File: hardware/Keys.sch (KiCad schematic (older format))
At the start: 1 part, among them U2 MCP23018_SSOP

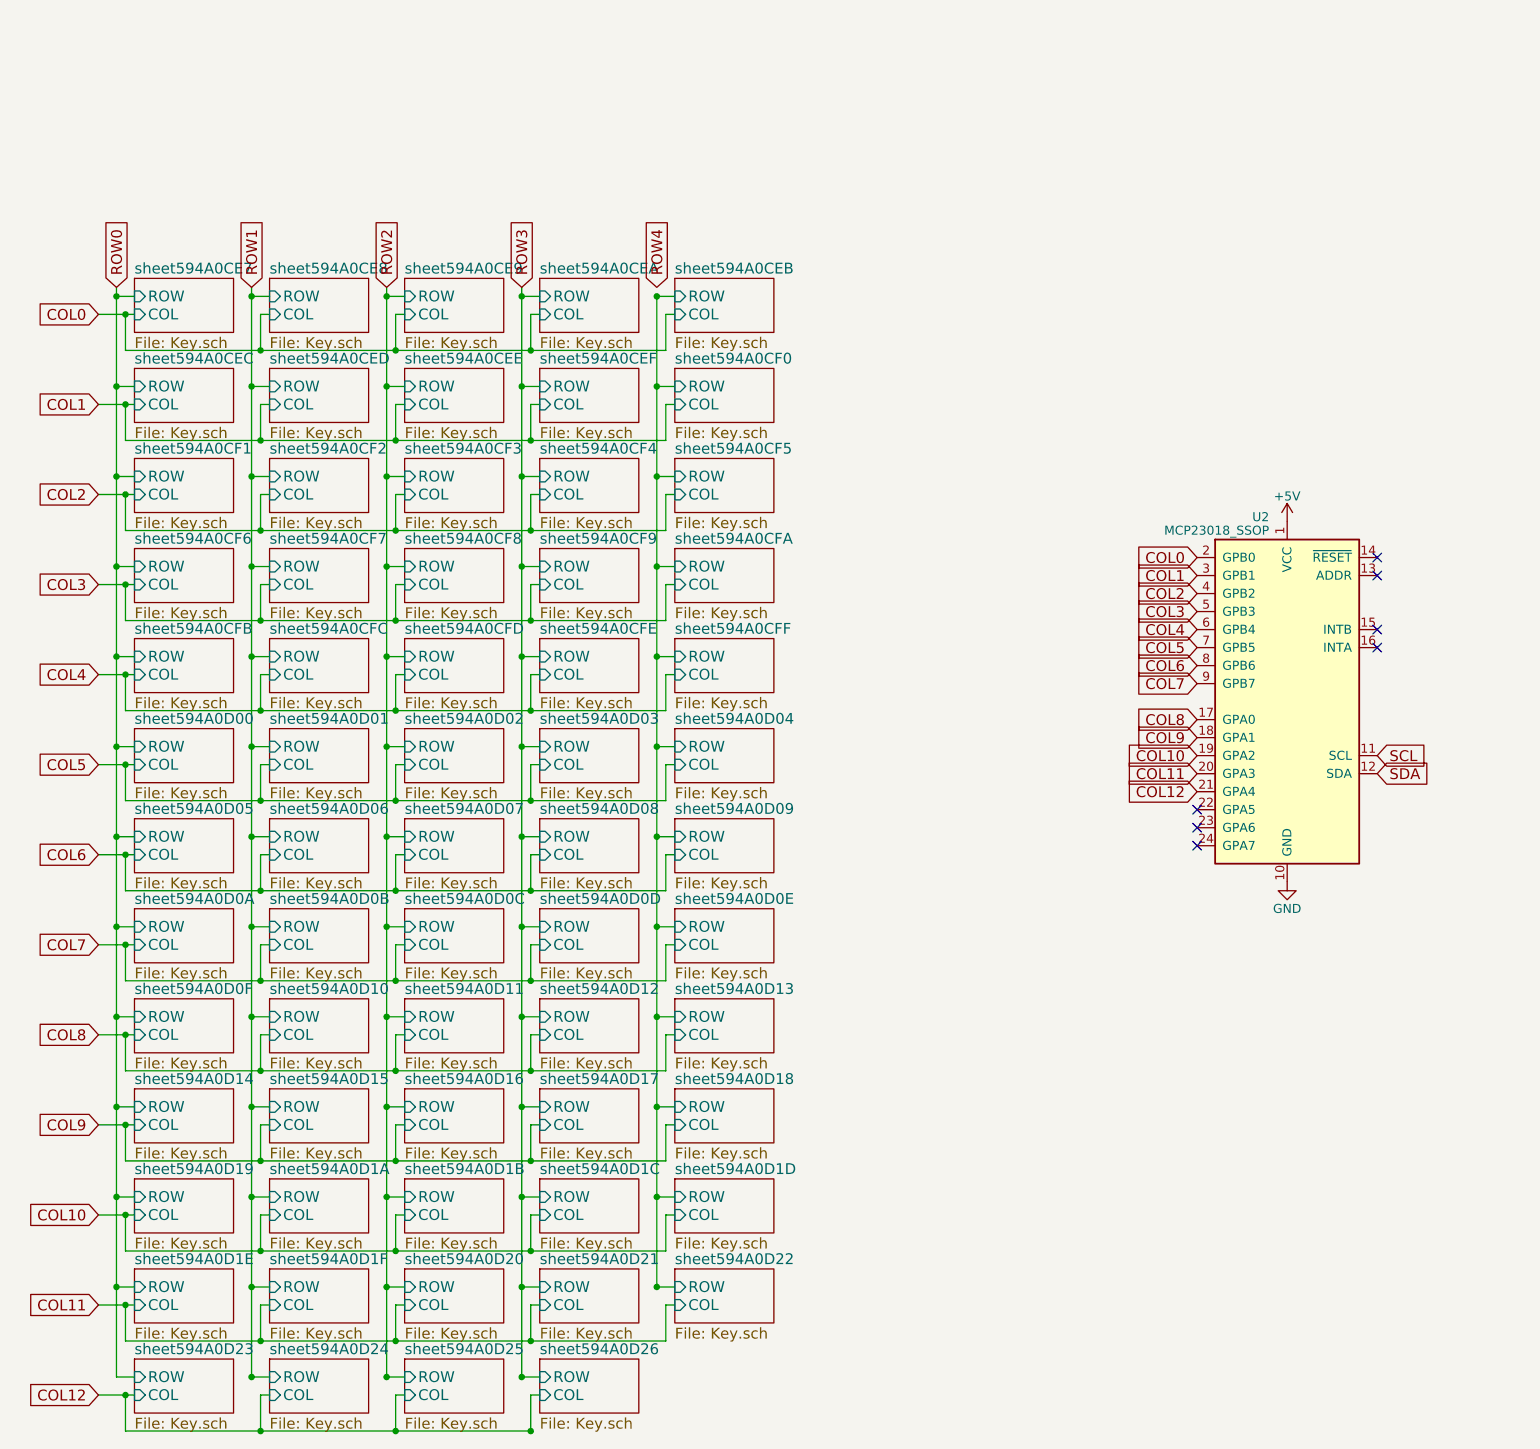
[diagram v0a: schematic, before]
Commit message: Add HWB, breakouts, LED to sch
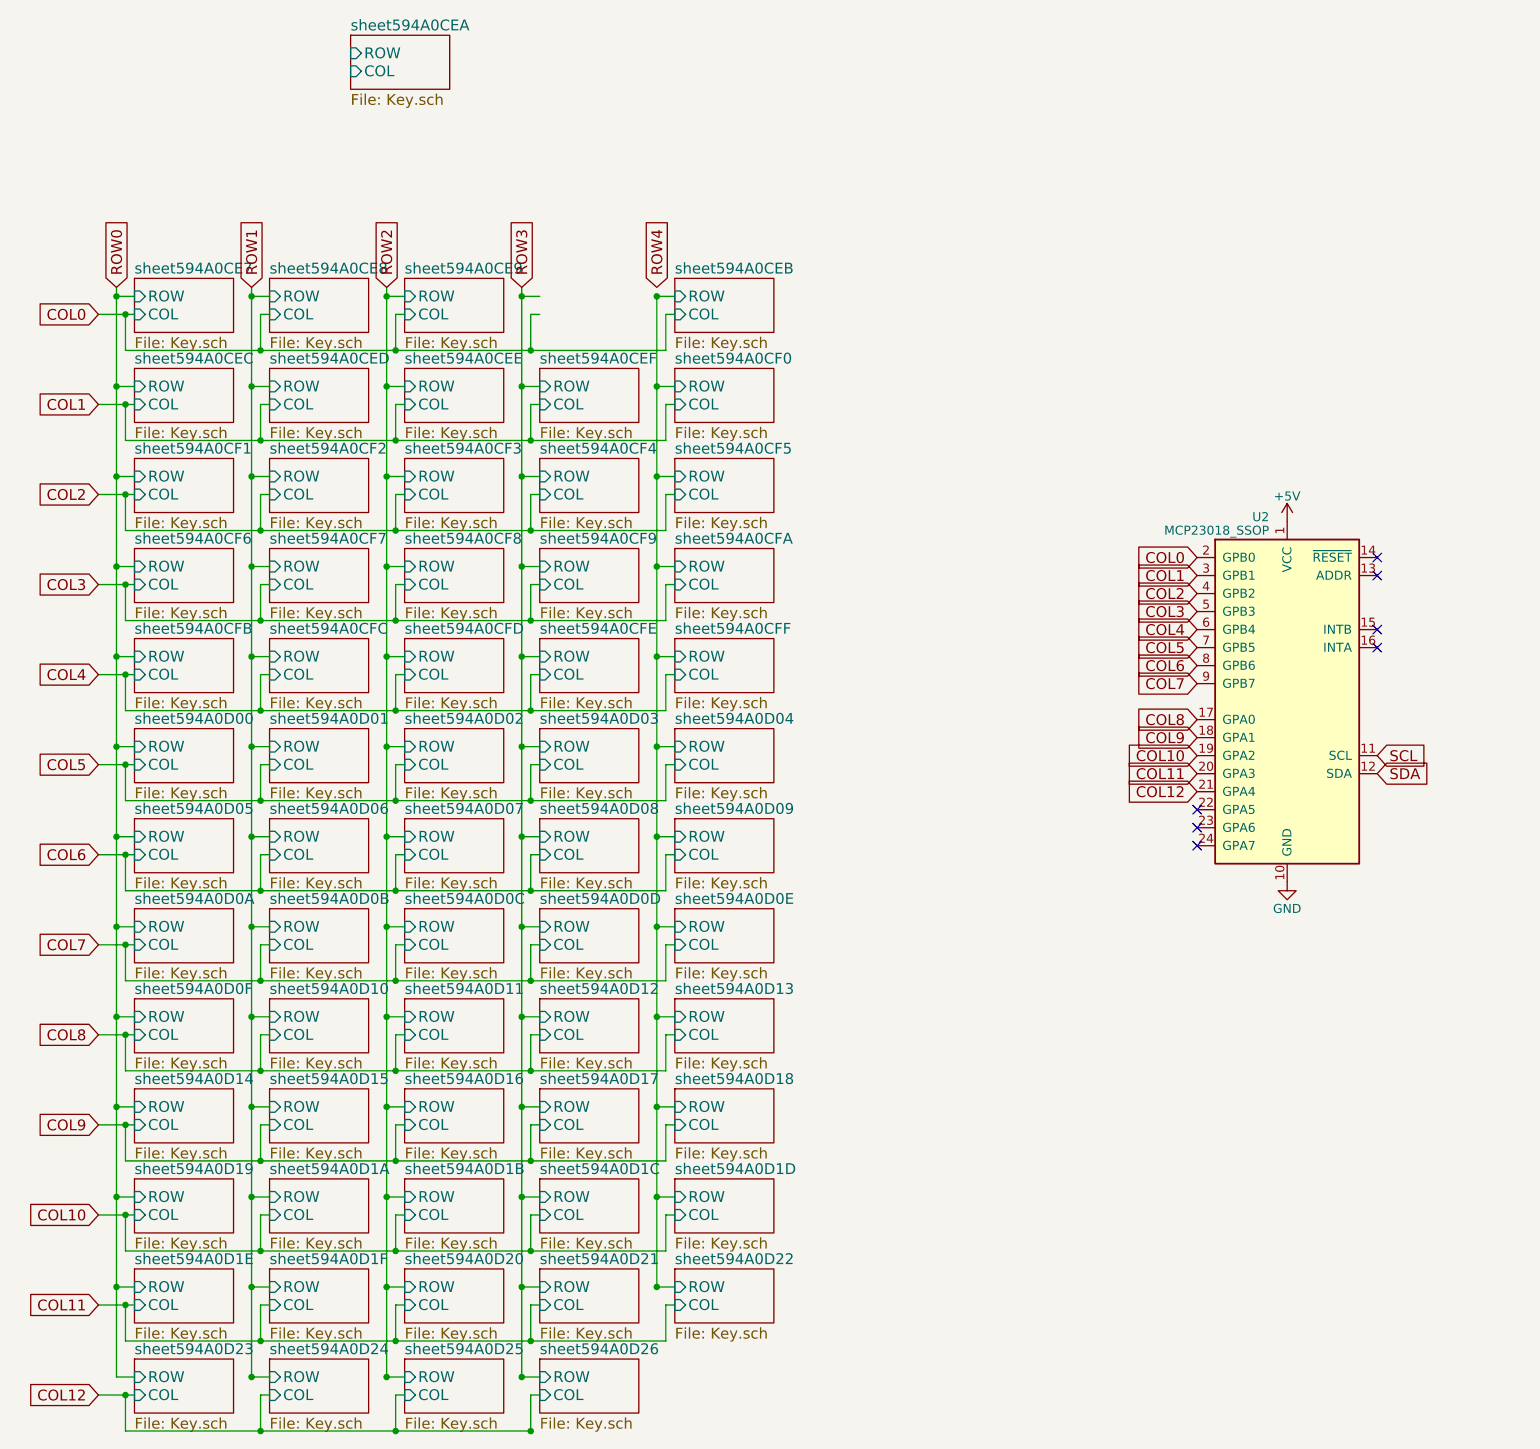
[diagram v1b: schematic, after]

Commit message: Move diodes in script, add big thumb buttons
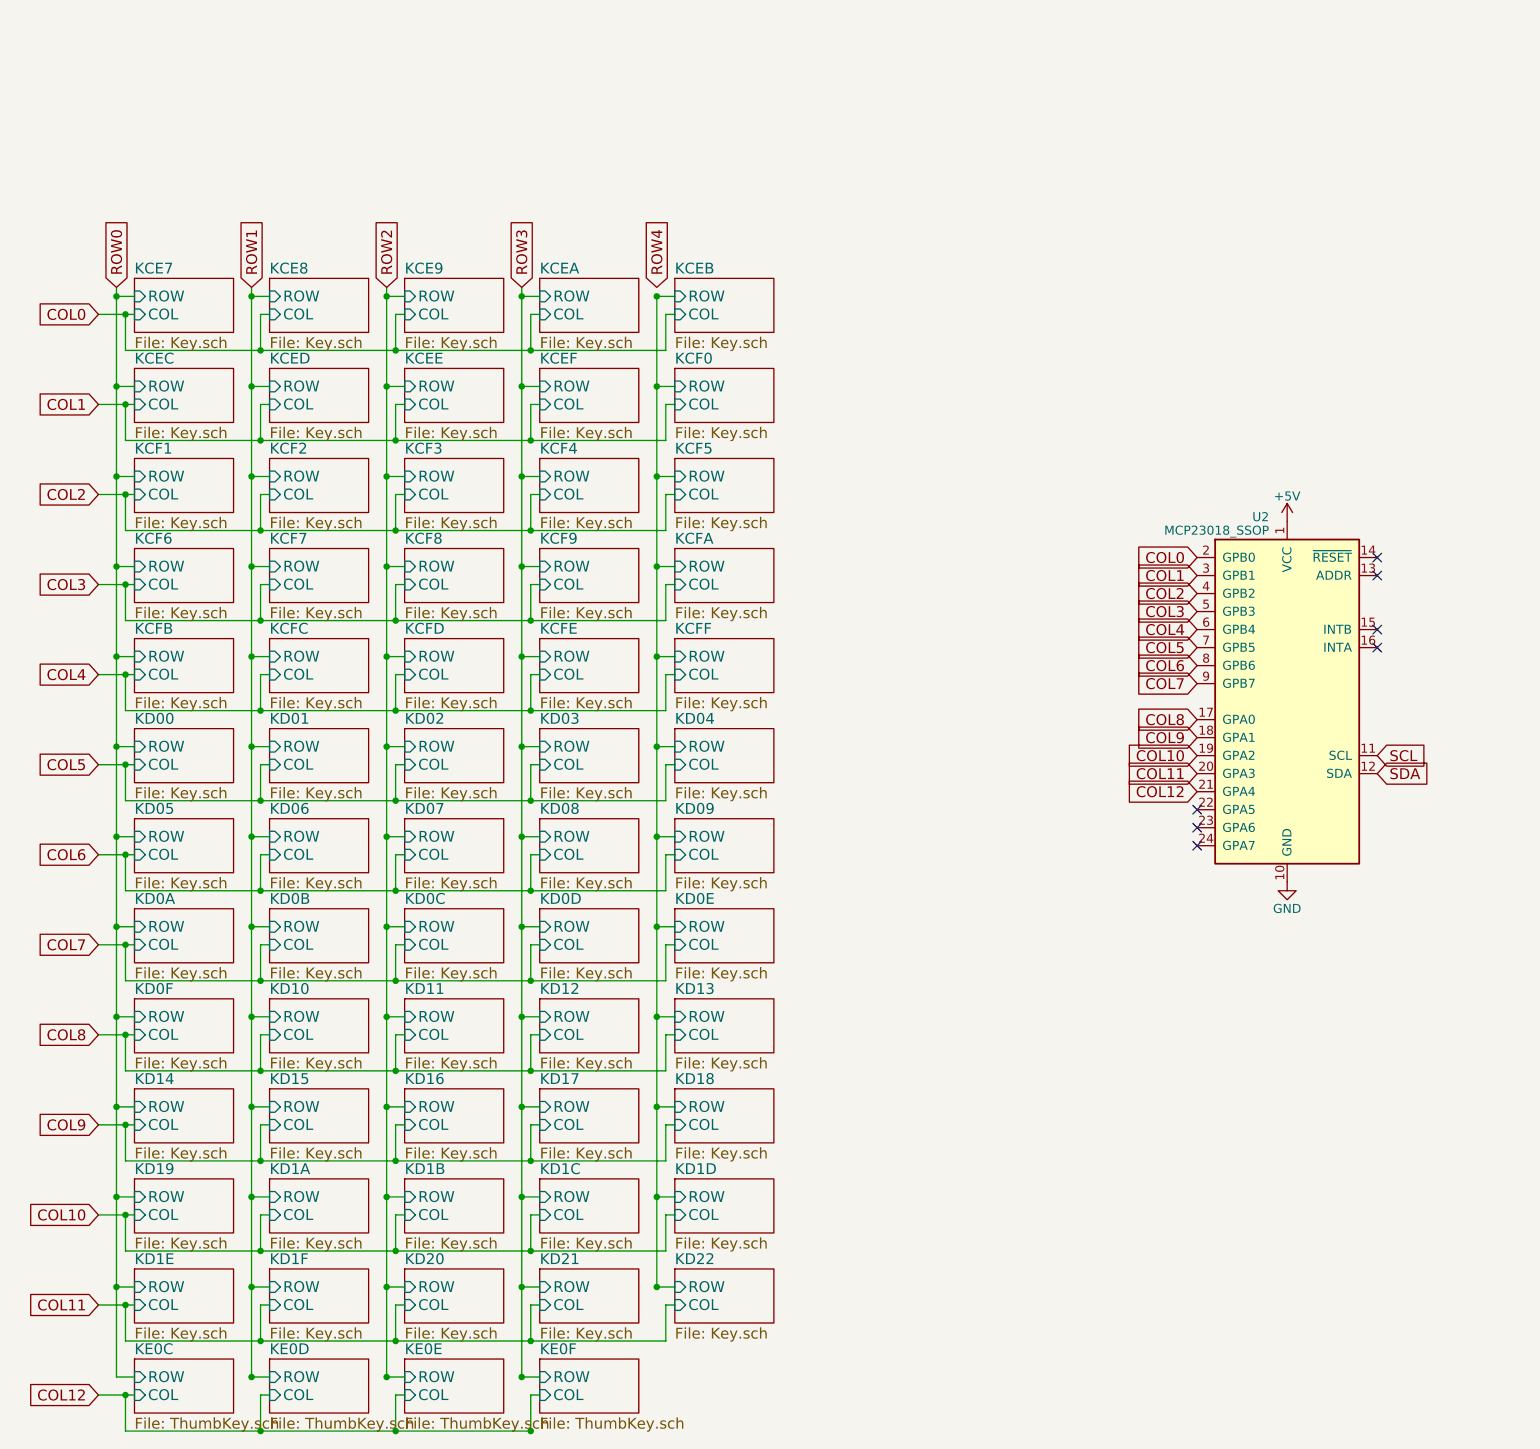
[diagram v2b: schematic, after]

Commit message: Fix diodes, Add board edge
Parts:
- added C5: 100nF, Capacitors_SMD:C_1206_HandSoldering, symbol C_Small
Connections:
- net +5V: now also C5.1
- net GND: now also C5.2
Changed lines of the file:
@@
 NoConn ~ 7300 4100
 $Comp
-L +5V #PWR016
+L +5V #PWR19
 U 1 1 594A3201
 P 7800 2300
-F 0 "#PWR016" H 7800 2150 50  0001 C CNN
+F 0 "#PWR19" H 7800 2150 50  0001 C CNN
 F 1 "+5V" H 7800 2440 50  0000 C CNN
 F 2 "" H 7800 2300 50  0001 C CNN
@@
 $EndComp
 $Comp
-L GND #PWR017
+L GND #PWR21
 U 1 1 594A3207
 P 7800 4300
-F 0 "#PWR017" H 7800 4050 50  0001 C CNN
+F 0 "#PWR21" H 7800 4050 50  0001 C CNN
 F 1 "GND" H 7800 4150 50  0000 C CNN
 F 2 "" H 7800 4300 50  0001 C CNN
@@
 F3 "COL" I L 3650 7150 60
 $EndSheet
+$Comp
+L C_Small C5
+U 1 1 5955CA14
+P 8850 2300
+F 0 "C5" H 8860 2370 50  0000 L CNN
+F 1 "100nF" H 8860 2220 50  0000 L CNN
+F 2 "Capacitors_SMD:C_1206_HandSoldering" H 8850 2300 50  0001 C CNN
+F 3 "" H 8850 2300 50  0001 C CNN
+	1    8850 2300
+	1    0    0    -1
+$EndComp
+$Comp
+L +5V #PWR18
+U 1 1 5955CD8D
+P 8850 2200
+F 0 "#PWR18" H 8850 2050 50  0001 C CNN
+F 1 "+5V" H 8850 2340 50  0000 C CNN
+F 2 "" H 8850 2200 50  0001 C CNN
+F 3 "" H 8850 2200 50  0001 C CNN
+	1    8850 2200
+	1    0    0    -1
+$EndComp
+$Comp
+L GND #PWR20
+U 1 1 5955D0A5
+P 8850 2400
+F 0 "#PWR20" H 8850 2150 50  0001 C CNN
+F 1 "GND" H 8850 2250 50  0000 C CNN
+F 2 "" H 8850 2400 50  0001 C CNN
+F 3 "" H 8850 2400 50  0001 C CNN
+	1    8850 2400
+	1    0    0    -1
+$EndComp
 $EndSCHEMATC

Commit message: Start routing
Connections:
- net COL10: now also U2.21 (GPA4); no longer U2.19 (GPA2)
- net COL11: now also U2.22 (GPA5); no longer U2.20 (GPA3)
- net COL12: now also U2.23 (GPA6); no longer U2.21 (GPA4)
- net COL6: now also U2.17 (GPA0); no longer U2.8 (GPB6)
- net COL7: now also U2.18 (GPA1); no longer U2.9 (GPB7)
- net COL8: now also U2.19 (GPA2); no longer U2.17 (GPA0)
- net COL9: now also U2.20 (GPA3); no longer U2.18 (GPA1)
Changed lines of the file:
@@
 Text GLabel 7300 3000 0    60   Input ~ 0
 COL5
-Text GLabel 7300 3100 0    60   Input ~ 0
+Text GLabel 7300 3400 0    60   Input ~ 0
 COL6
-Text GLabel 7300 3200 0    60   Input ~ 0
+Text GLabel 7300 3500 0    60   Input ~ 0
 COL7
-Text GLabel 7300 3400 0    60   Input ~ 0
+Text GLabel 7300 3600 0    60   Input ~ 0
 COL8
-Text GLabel 7300 3500 0    60   Input ~ 0
+Text GLabel 7300 3700 0    60   Input ~ 0
 COL9
-Text GLabel 7300 3600 0    60   Input ~ 0
+Text GLabel 7300 3800 0    60   Input ~ 0
 COL10
-Text GLabel 7300 3700 0    60   Input ~ 0
+Text GLabel 7300 3900 0    60   Input ~ 0
 COL11
-Text GLabel 7300 3800 0    60   Input ~ 0
+Text GLabel 7300 4000 0    60   Input ~ 0
 COL12
-NoConn ~ 7300 3900
-NoConn ~ 7300 4000
 NoConn ~ 7300 4100
 $Comp
@@
 	1    0    0    -1
 $EndComp
+NoConn ~ 7300 3100
+NoConn ~ 7300 3200
 $EndSCHEMATC

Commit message: WIP for V2 fixes
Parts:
- U2: footprint Housings_SSOP:SSOP-28_5.3x10.2mm_Pitch0.65mm -> Housings_SSOP:SSOP-24_5.3x8.2mm_Pitch0.65mm
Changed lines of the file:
@@
 LIBS:valves
 LIBS:keyboard-cache
-EELAYER 26 0
+EELAYER 25 0
 EELAYER END
 $Descr A4 11693 8268
@@
 NoConn ~ 7300 4100
 $Comp
-L +5V #PWR018
+L +5V #PWR015
 U 1 1 594A3201
 P 7800 2300
-F 0 "#PWR018" H 7800 2150 50  0001 C CNN
+F 0 "#PWR015" H 7800 2150 50  0001 C CNN
 F 1 "+5V" H 7800 2440 50  0000 C CNN
 F 2 "" H 7800 2300 50  0001 C CNN
@@
 $EndComp
 $Comp
-L GND #PWR019
+L GND #PWR016
 U 1 1 594A3207
 P 7800 4300
-F 0 "#PWR019" H 7800 4050 50  0001 C CNN
+F 0 "#PWR016" H 7800 4050 50  0001 C CNN
 F 1 "GND" H 7800 4150 50  0000 C CNN
 F 2 "" H 7800 4300 50  0001 C CNN
@@
 F 0 "U2" H 7700 4325 50  0000 R CNN
 F 1 "MCP23018_SSOP" H 7700 4250 50  0000 R CNN
-F 2 "Housings_SSOP:SSOP-28_5.3x10.2mm_Pitch0.65mm" H 7850 2350 50  0001 L CNN
+F 2 "Housings_SSOP:SSOP-24_5.3x8.2mm_Pitch0.65mm" H 7850 2350 50  0001 L CNN
 F 3 "" H 8050 4300 50  0001 C CNN
 	1    7800 3300
@@
 $EndComp
 $Comp
-L +5V #PWR020
+L +5V #PWR017
 U 1 1 5955CD8D
 P 8850 2200
-F 0 "#PWR020" H 8850 2050 50  0001 C CNN
+F 0 "#PWR017" H 8850 2050 50  0001 C CNN
 F 1 "+5V" H 8850 2340 50  0000 C CNN
 F 2 "" H 8850 2200 50  0001 C CNN
@@
 $EndComp
 $Comp
-L GND #PWR021
+L GND #PWR018
 U 1 1 5955D0A5
 P 8850 2400
-F 0 "#PWR021" H 8850 2150 50  0001 C CNN
+F 0 "#PWR018" H 8850 2150 50  0001 C CNN
 F 1 "GND" H 8850 2250 50  0000 C CNN
 F 2 "" H 8850 2400 50  0001 C CNN
